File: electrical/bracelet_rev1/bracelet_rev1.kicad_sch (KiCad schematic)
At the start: 21 parts, among them U1 nRF54L10-QFXX, Y1 Crystal_GND24

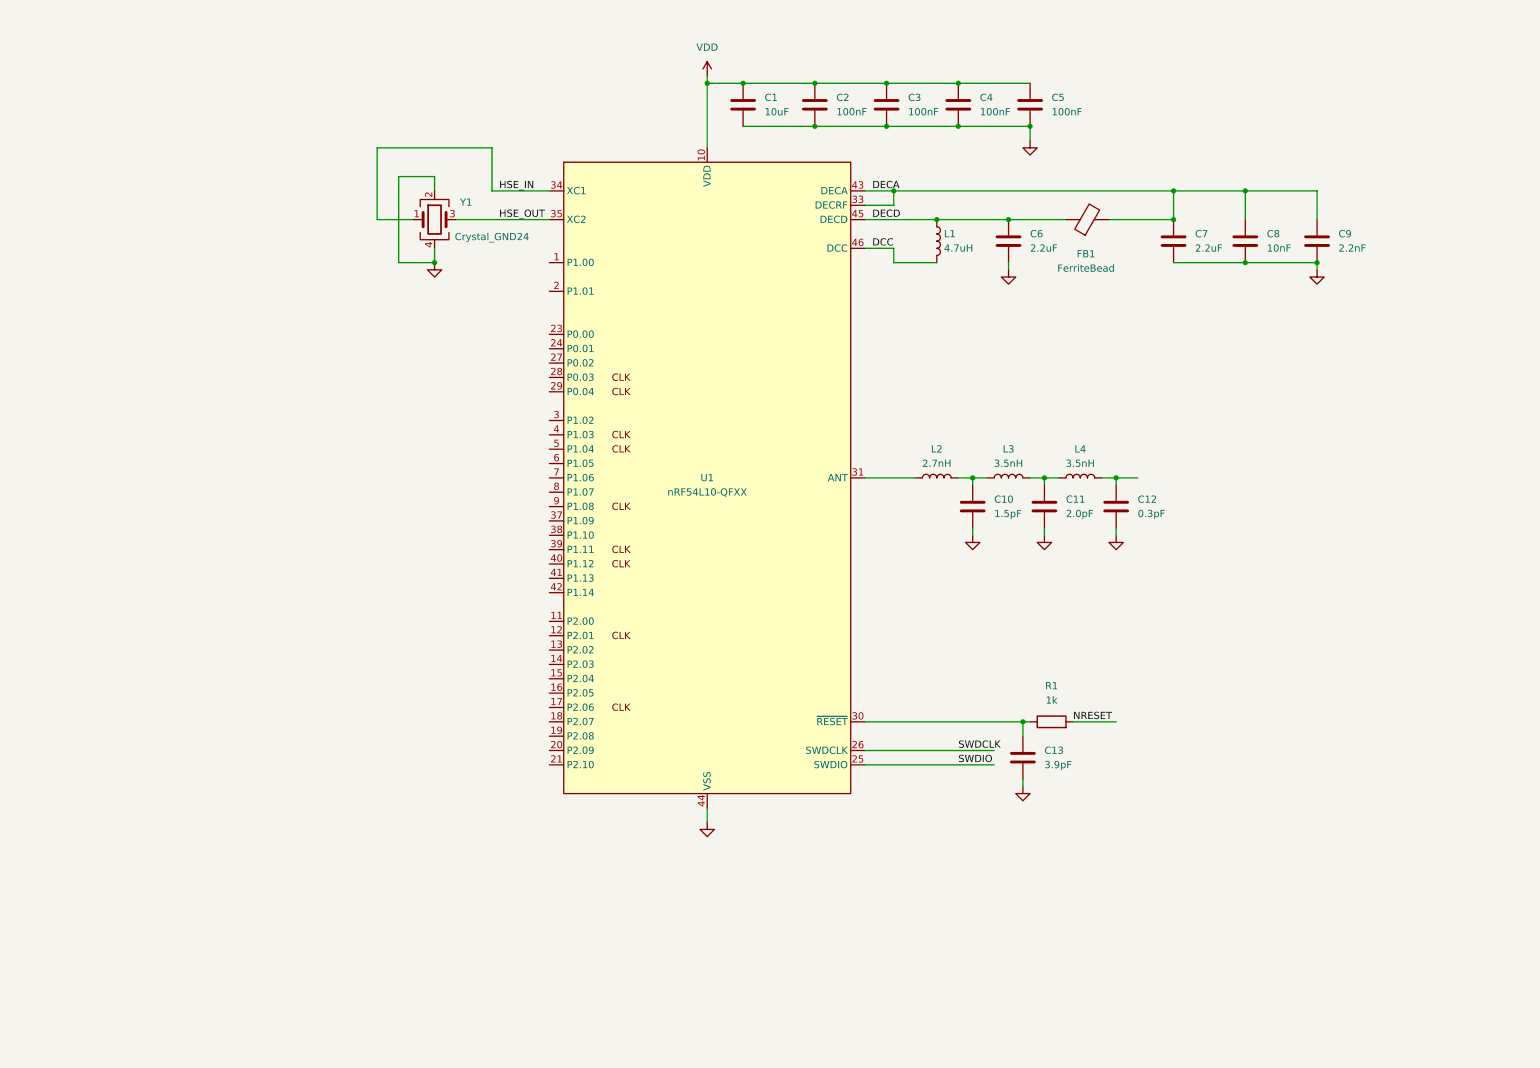
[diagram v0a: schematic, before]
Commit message: Add IMU to schematic
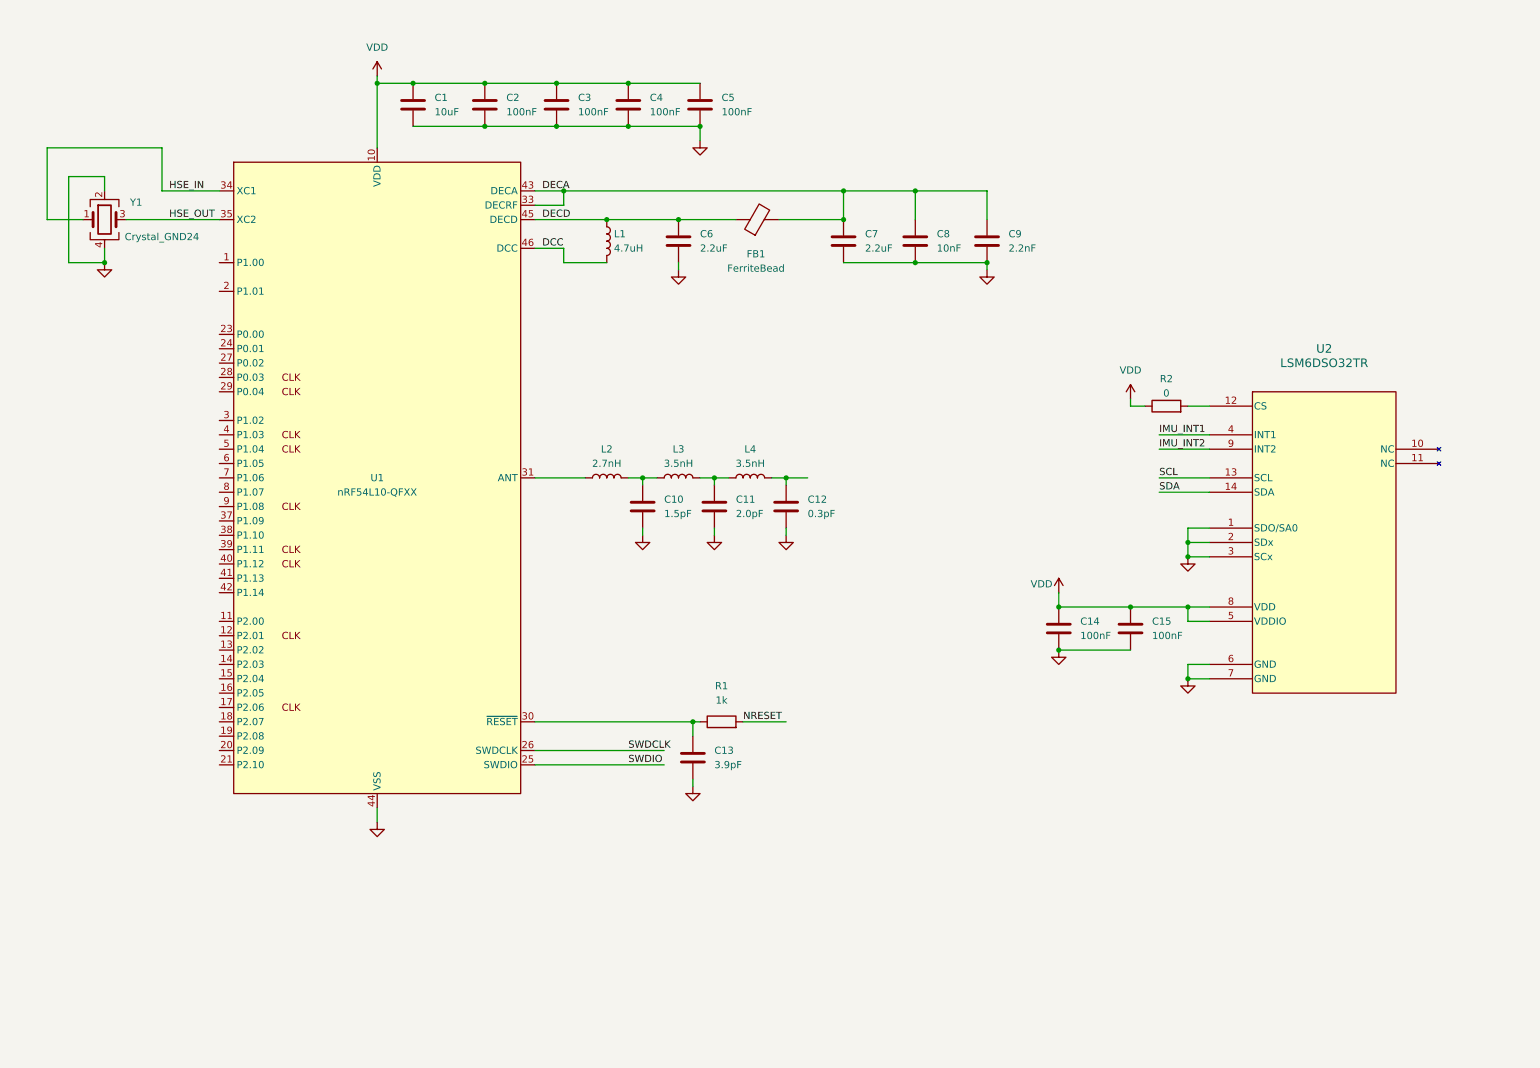
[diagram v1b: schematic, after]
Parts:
- added C14, C15: 100nF, symbol Device:C
- added R2: 0, symbol Device:R
- added U2: LSM6DSO32TR, LGA-14L_2P5X3X0P83_STM, symbol IMU:LSM6DSO32TR
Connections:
- net GND: now also C14.2, C15.2, U2.1 (SDO/SA0), U2.2 (SDx), U2.3 (SCx), U2.6 (GND), U2.7 (GND)
- net VDD: now also C14.1, C15.1, R2.1, U2.5 (VDDIO), U2.8 (VDD)
- new net: R2.2, U2.12 (CS)
- new net IMU_INT1: U2.4 (INT1)
- new net IMU_INT2: U2.9 (INT2)
- new net SCL: U2.13 (SCL)
- new net SDA: U2.14 (SDA)
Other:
- moved on the sheet: C1, C10, C11, C12, C13, C2, C3, C4, C5, C6, C7, C8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

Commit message: Added power. It is a mess
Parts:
- added C16: 4.7uF, symbol Device:C
- added C17: 10uF, symbol Device:C
- added C18, C19: 2.2uF, symbol Device:C
- added D1: LED, symbol Device:LED
- added D2: D_Schottky, symbol Device:D_Schottky
- added J1: USB_C_Receptacle_USB2.0_14P, symbol Connector:USB_C_Receptacle_USB2.0_14P
- added Q1: PMOS, symbol Simulation_SPICE:PMOS
- added R3, R4, R5: 5.1k, symbol Device:R
- added R6, R7, R8: 10k, symbol Device:R
- added U3: MCP73831T-2ACI/OT, SOT-23-5_MC_MCH, symbol Battery Manager:MCP73831T-2ACI_OT
- added U4: XC6222B331MR-G, SOT-25_TOR, symbol LDO:XC6222B331MR-G
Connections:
- net GND: now also C16.2, C17.2, C18.2, C19.2, J1.A1 (GND), J1.A12 (GND), J1.B1 (GND), J1.B12 (GND), J1.S1 (SHIELD), R3.2, R4.2, R6.2, R7.1, U3.2 (VSS), U4.2 (VSS)
- net VDD: now also C18.1, U4.5 (VOUT)
- new net: J1.A5 (CC1), R4.1
- new net: C19.1, D2.1 (K), Q1.3 (S), R8.2, U4.1 (VIN)
- new net: R6.1, U3.5 (PROG)
- new net: D1.1 (K), U3.1 (STAT)
- new net: J1.B5 (CC2), R3.1
- new net: R8.1, U4.3 (CE)
- new net: D1.2 (A), R5.2
- new net +BATT: C17.1, Q1.1 (D), U3.3 (VBAT)
- new net USB_D+: J1.A6 (D+), J1.B6 (D+)
- new net USB_D-: J1.A7 (D-), J1.B7 (D-)
- new net USB_VBUS: C16.1, D2.2 (A), J1.A4 (VBUS), J1.A9 (VBUS), J1.B4 (VBUS), J1.B9 (VBUS), Q1.2 (G), R5.1, R7.2, U3.4 (VDD)
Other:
- note added: "Note: Maybe add reverse current protection here?"
- note added: "Note: Not sure what Cin should be"
- note added: "See Figure 2-4 of datasheet for Charge Current vs PROG curve"
- moved on the sheet: C1, C10, C11, C12, C13, C14, C15, C2, C3, C4, C5, C6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

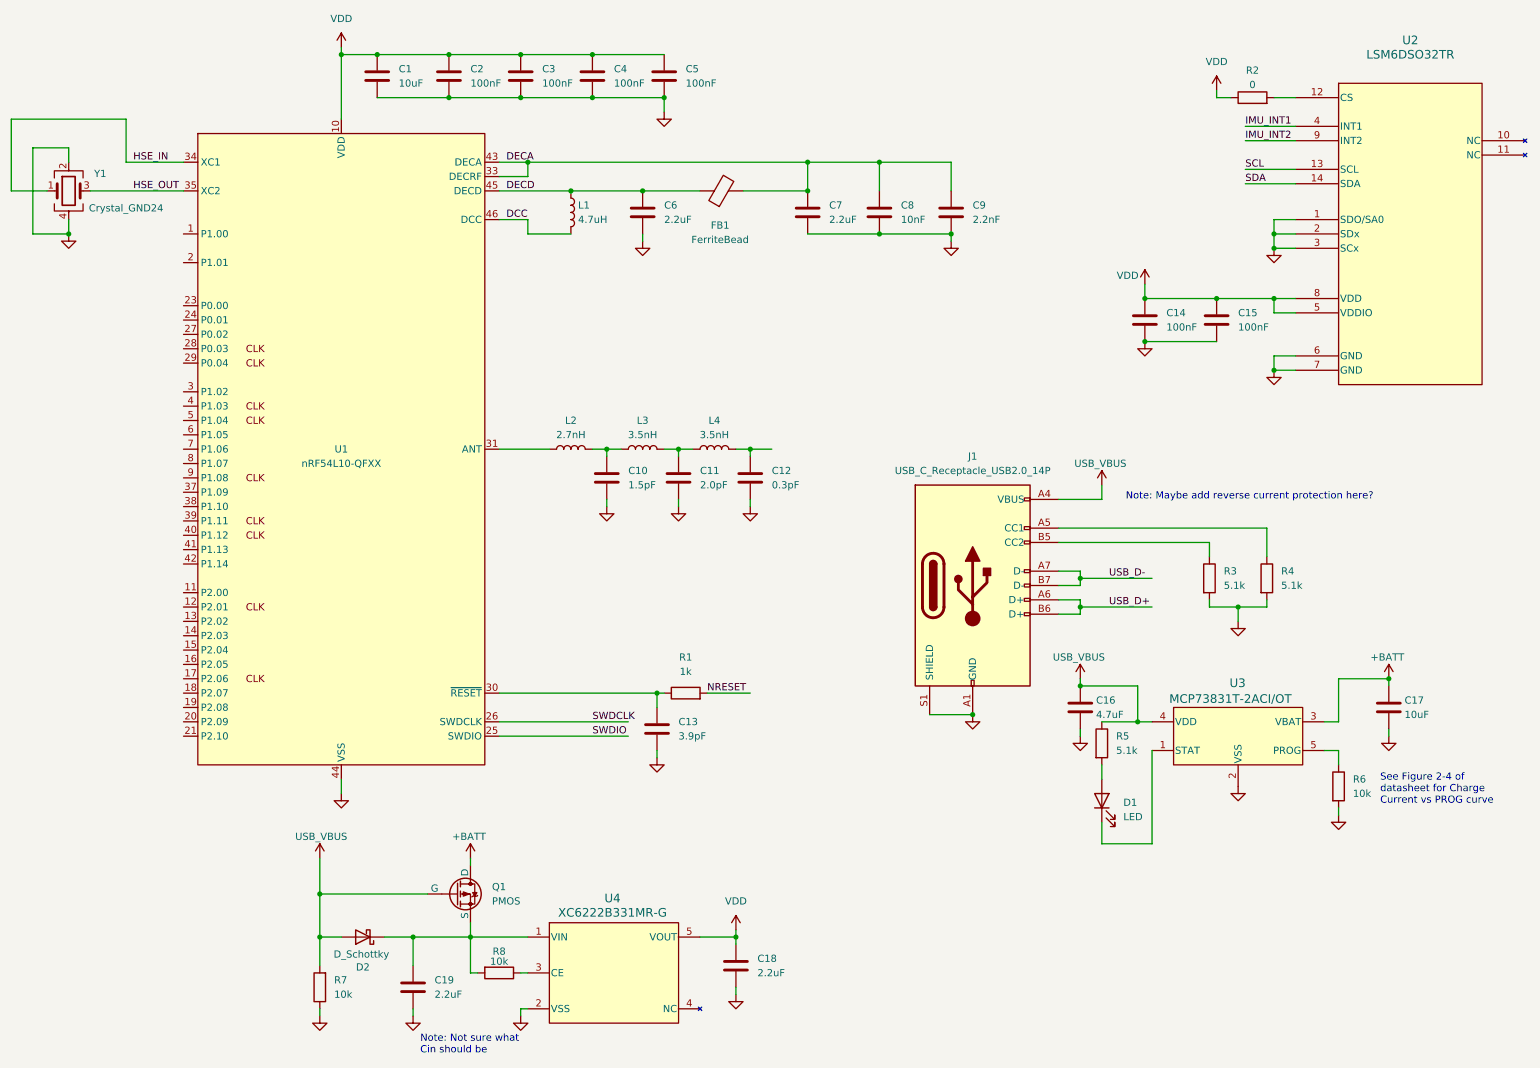
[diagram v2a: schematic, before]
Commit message: Organize schematic a bit
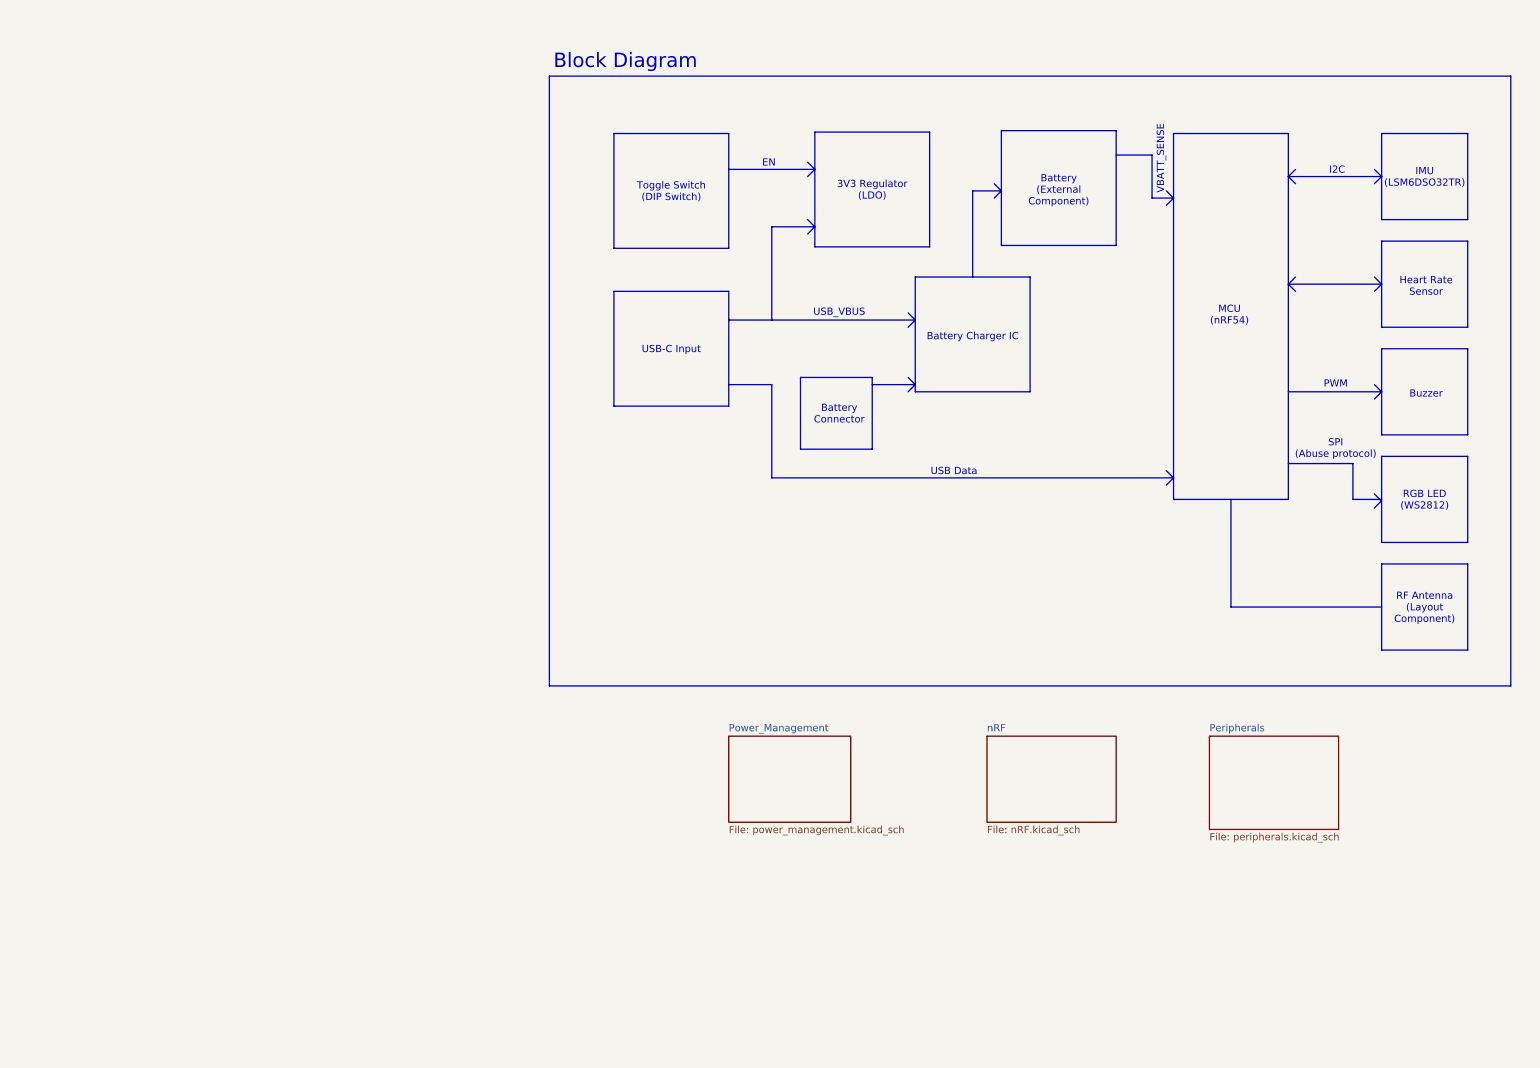
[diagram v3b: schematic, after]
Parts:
- removed C1, C17: 10uF, symbol Device:C
- removed C10: 1.5pF, symbol Device:C
- removed C11: 2.0pF, symbol Device:C
- removed C12: 0.3pF, symbol Device:C
- removed C13: 3.9pF, symbol Device:C
- removed C14, C15, C2, C3, C4, C5: 100nF, symbol Device:C
- removed C16: 4.7uF, symbol Device:C
- removed C18, C19, C6, C7: 2.2uF, symbol Device:C
- removed C8: 10nF, symbol Device:C
- removed C9: 2.2nF, symbol Device:C
- removed D1: LED, symbol Device:LED
- removed D2: D_Schottky, symbol Device:D_Schottky
- removed FB1: FerriteBead, symbol Device:FerriteBead
- removed J1: USB_C_Receptacle_USB2.0_14P, symbol Connector:USB_C_Receptacle_USB2.0_14P
- removed L1: 4.7uH, symbol Device:L
- removed L2: 2.7nH, symbol Device:L
- removed L3, L4: 3.5nH, symbol Device:L
- removed Q1: PMOS, symbol Simulation_SPICE:PMOS
- removed R1: 1k, symbol Device:R
- removed R2: 0, symbol Device:R
- removed R3, R4, R5: 5.1k, symbol Device:R
- removed R6, R7, R8: 10k, symbol Device:R
- removed U1: nRF54L10-QFXX, Package_DFN_QFN:QFN-48-1EP_6x6mm_P0.4mm_EP4.6x4.6mm, symbol PCM_nordic-lib-kicad-nrf54l:nRF54L10-QFXX
- removed U2: LSM6DSO32TR, LGA-14L_2P5X3X0P83_STM, symbol IMU:LSM6DSO32TR
- removed U3: MCP73831T-2ACI/OT, SOT-23-5_MC_MCH, symbol Battery Manager:MCP73831T-2ACI_OT
- removed U4: XC6222B331MR-G, SOT-25_TOR, symbol LDO:XC6222B331MR-G
- removed Y1: Crystal_GND24, symbol Device:Crystal_GND24
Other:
- added sheet Peripherals (peripherals.kicad_sch)
- added sheet Power_Management (power_management.kicad_sch)
- added sheet nRF (nRF.kicad_sch)
- note added: "3V3 Regulator (LDO)"
- note added: "Battery (External Component)"
- note added: "Battery Charger IC"
- note added: "Battery Connector"
- note added: "Block Diagram"
- note added: "Buzzer"
- note added: "EN"
- note added: "Heart Rate Sensor"
- note added: "I2C"
- note added: "IMU (LSM6DSO32TR)"
- note added: "MCU (nRF54)"
- note added: "PWM"
- note added: "RF Antenna (Layout Component)"
- note added: "RGB LED (WS2812)"
- note added: "SPI (Abuse protocol)"
- note added: "Toggle Switch (DIP Switch)"
- note added: "USB Data"
- note added: "USB-C Input"
- note added: "USB_VBUS"
- note added: "VBATT_SENSE"
- note removed: "Note: Maybe add reverse current protection here?"
- note removed: "Note: Not sure what Cin should be"
- note removed: "See Figure 2-4 of datasheet for Charge Current vs PROG curve"
